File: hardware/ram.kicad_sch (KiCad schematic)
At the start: 17 parts, among them U10 IS42S16320D-6BLI, U4 CCGM1A1

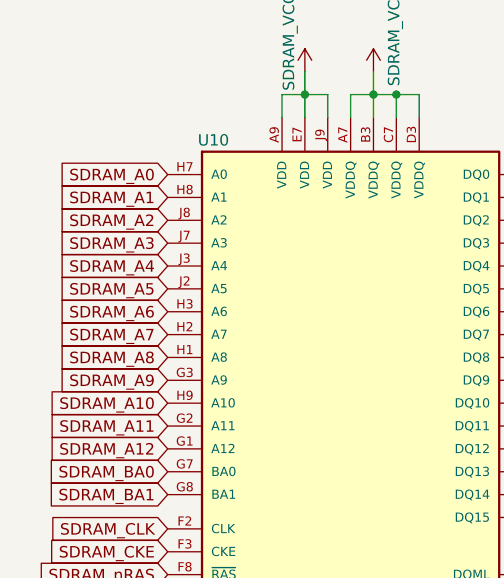
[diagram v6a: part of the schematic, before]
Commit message: Routing GPDI
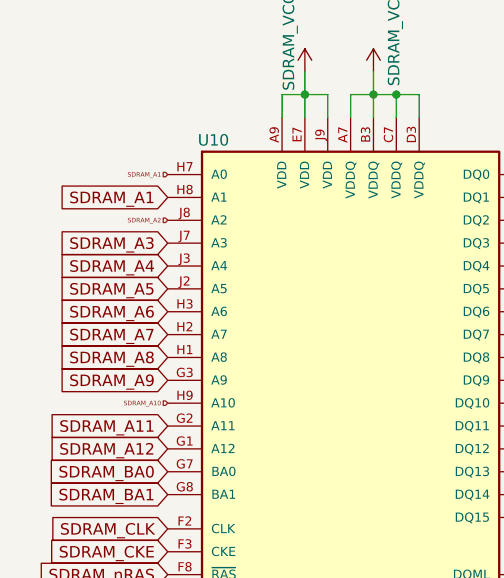
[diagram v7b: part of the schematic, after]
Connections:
- net SDRAM_A0: no longer U10.H7 (A0)
- net SDRAM_A1: now also U10.H7 (A0)

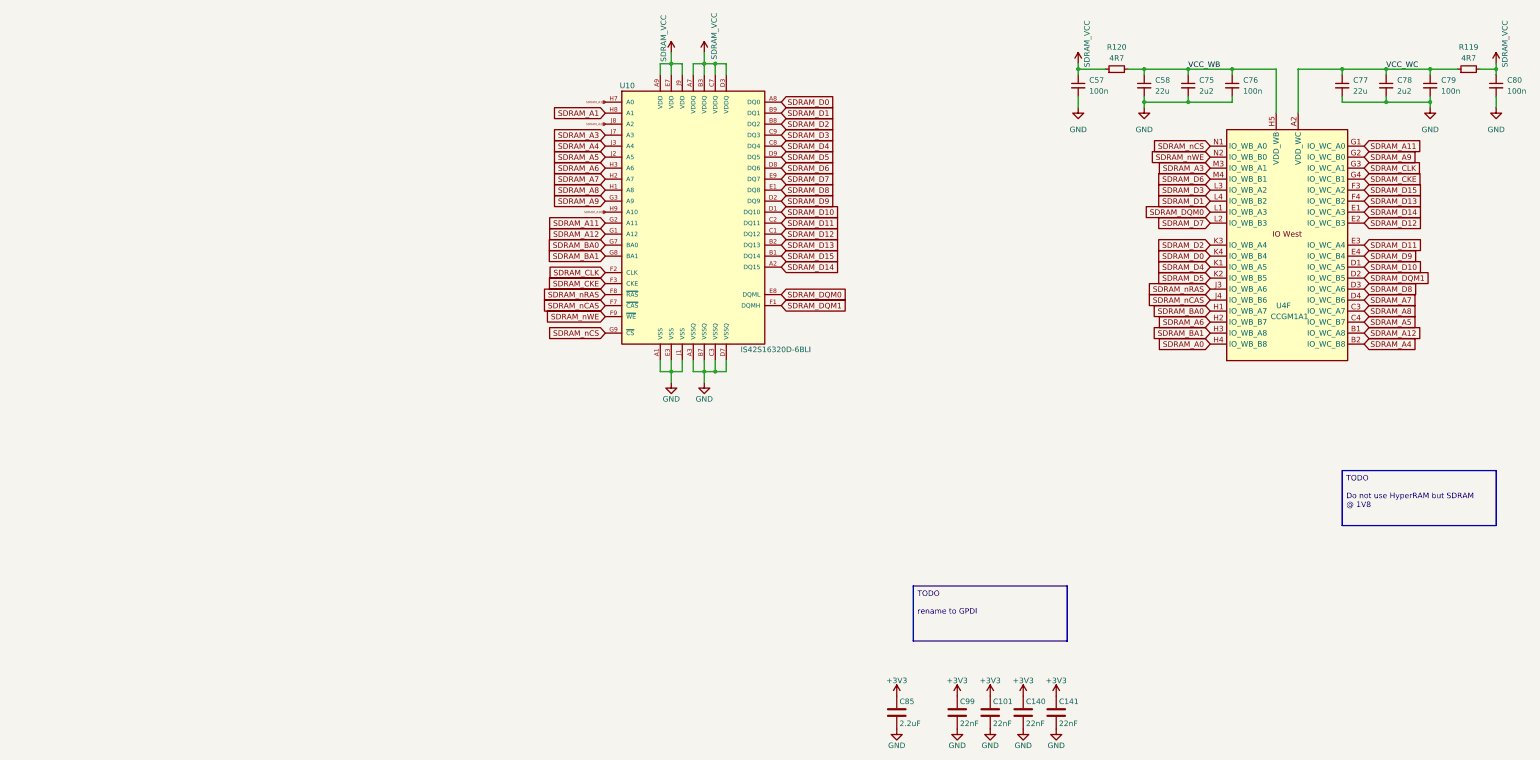
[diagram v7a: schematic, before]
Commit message: Clearing ERC errors/warnings
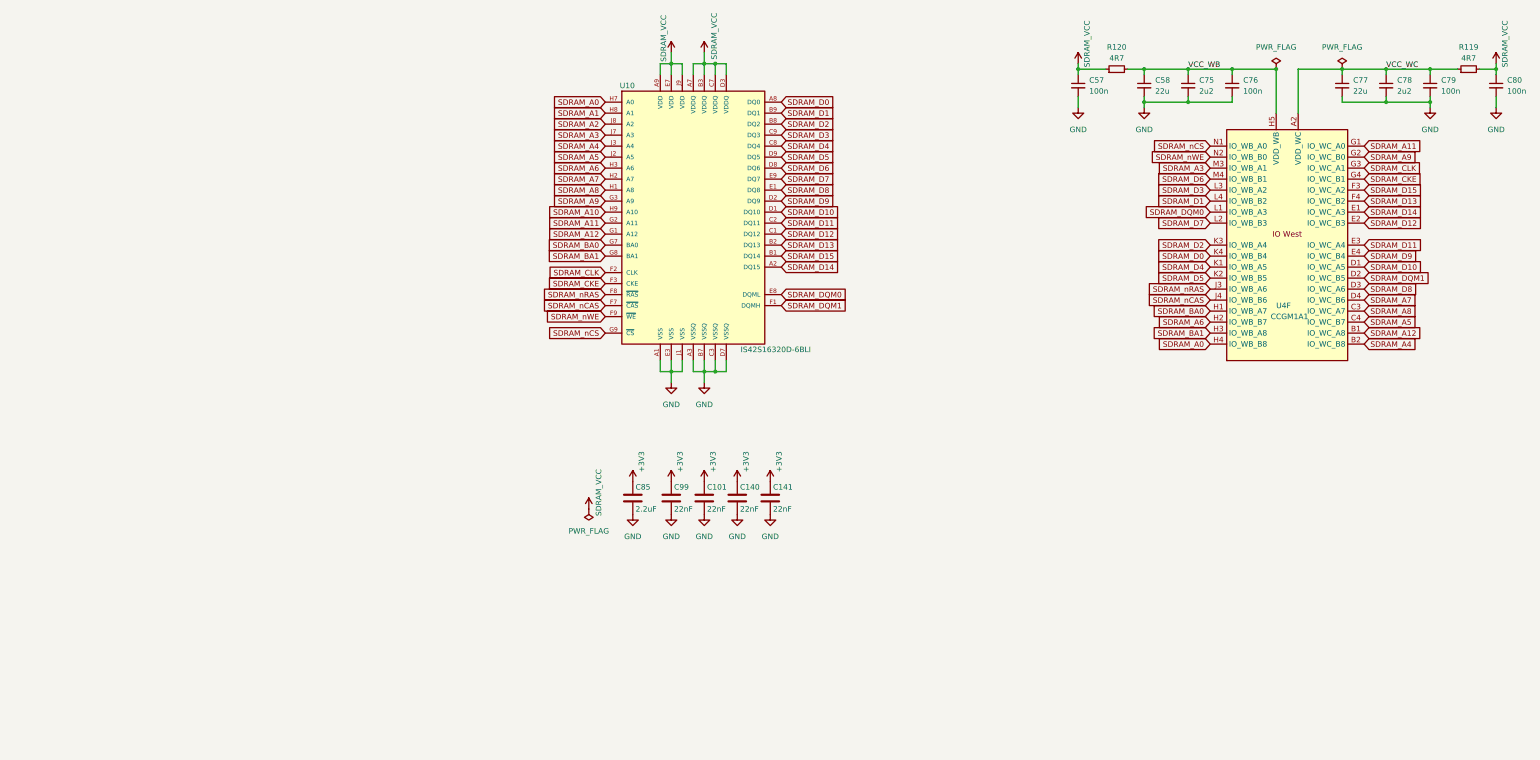
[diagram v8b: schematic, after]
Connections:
- net SDRAM_A0: now also U10.H7 (A0)
- net SDRAM_A1: no longer U10.H7 (A0)
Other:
- moved on the sheet: C101, C140, C141, C85, C99
